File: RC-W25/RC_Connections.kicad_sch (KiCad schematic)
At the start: 26 parts, among them J1 USB_C_Receptacle_USB2.0_14P, SW3 Button, SW4 Button, U1 ESP32-C6-WROOM-1

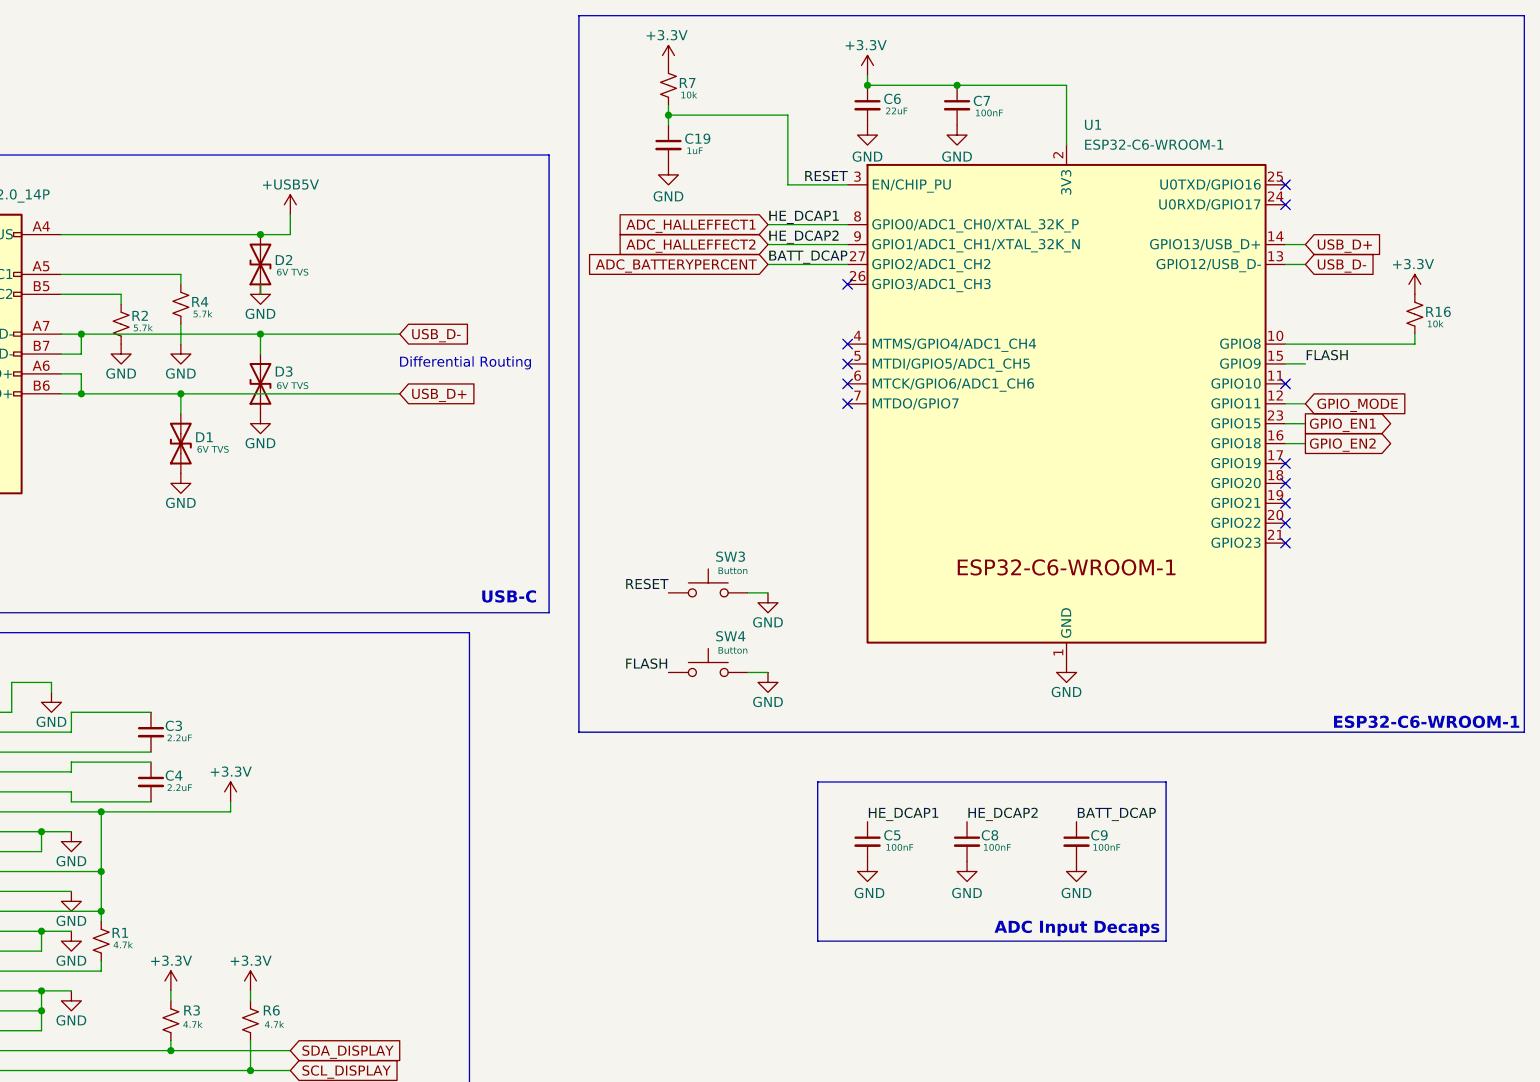
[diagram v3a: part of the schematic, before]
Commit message: Began Routing
Only need to spec out buttons before completion
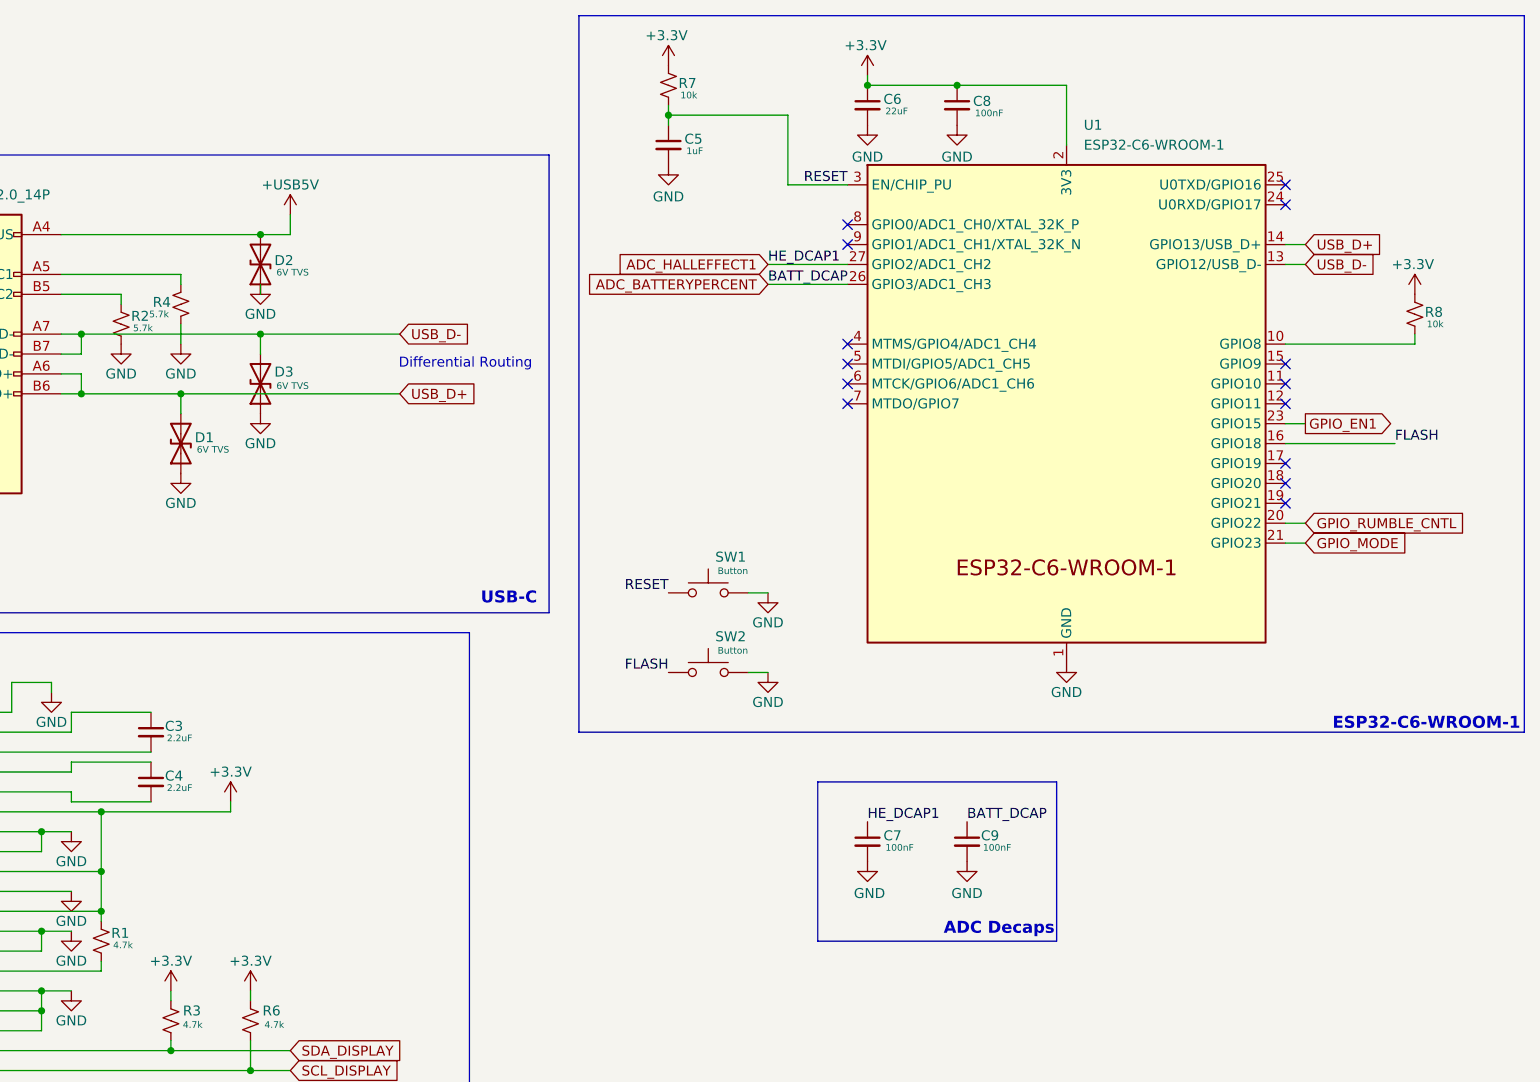
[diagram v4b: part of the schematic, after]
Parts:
- removed C8: 100nF, Capacitor_SMD:C_0402_1005Metric, symbol Device:C_Small
- R7: LCSC# C852861 -> C190095
- R8: renamed from R16; LCSC# C852861 -> C190095
- U1: footprint PCM_Espressif:ESP32-C6-WROOM-1 -> RF_Module:ESP32-C6-MINI-1
- renumbered C19 to C5, C5 to C7, C7 to C8, SW3 to SW1, SW4 to SW2
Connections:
- net GPIO_EN2 is gone; now on net FLASH: U1.16 (GPIO18)
- net ADC_BATTERYPERCENT: now also U1.26 (GPIO3/ADC1_CH3); no longer U1.27 (GPIO2/ADC1_CH2)
- net ADC_HALLEFFECT1: now also U1.27 (GPIO2/ADC1_CH2); no longer U1.8 (GPIO0/ADC1_CH0/XTAL_32K_P)
- net FLASH: no longer U1.15 (GPIO9)
- net GPIO_MODE: now also U1.21 (GPIO23); no longer U1.12 (GPIO11)
- net GPIO_RUMBLE_CNTL: now reaches U1.20 (GPIO22)
- net ADC_HALLEFFECT2: no longer names the net of U1.9 (GPIO1/ADC1_CH1/XTAL_32K_N)
- no-connect marks 14 -> 15
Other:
- note added: "ADC Decaps"
- note removed: "ADC Input Decaps"
- moved on the sheet: C9

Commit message: EM Custom RC V1
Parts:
- added H1, H2, H3, H4: MountingHole, MountingHole:MountingHole_2.2mm_M2, symbol Mechanical:MountingHole
- DS1: LCSC# (none) -> C2856808
- SW1, SW2: footprint (none) -> footprints:SW-SMD_L3.9-W3.0-P4.45; LCSC# (none) -> C720477
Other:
- note added: "MH"

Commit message: crc v1
finalized!! finally!! yes!!

- spec out 3.7V 1000mAh cell
- spec out ultra-thin coin motor

^make sure they have a jst-ph male connector or are organized to be ordered alongside one for manual soldering.
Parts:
- removed H1: MountingHole, MountingHole:MountingHole_2.2mm_M2, symbol Mechanical:MountingHole
- H1: renamed from H2; footprint MountingHole:MountingHole_2.2mm_M2 -> MountingHole:MountingHole_3.2mm_M3
- H2: renamed from H3; footprint MountingHole:MountingHole_2.2mm_M2 -> MountingHole:MountingHole_3.2mm_M3
- H3: renamed from H4; footprint MountingHole:MountingHole_2.2mm_M2 -> MountingHole:MountingHole_3.2mm_M3
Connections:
- net GPIO_EN1: now also U1.21 (GPIO23); no longer U1.23 (GPIO15)
- net GPIO_MODE: now also U1.20 (GPIO22); no longer U1.21 (GPIO23)
- net GPIO_RUMBLE_CNTL: now also U1.23 (GPIO15); no longer U1.20 (GPIO22)
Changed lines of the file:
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@@
 	(wire
 		(pts
-			(xy 234.95 69.85) (xy 220.98 69.85)
+			(xy 245.11 69.85) (xy 220.98 69.85)
 		)
 		(stroke
@@
 	)
 	(rectangle
-		(start 139.7 156.21)
+		(start 139.7 161.29)
 		(end 158.75 179.07)
 		(stroke
@@
 	)
 	(label "FLASH"
-		(at 234.95 69.85 0)
+		(at 245.11 69.85 0)
 		(effects
 			(font
@@
 		)
 	)
-	(global_label "GPIO_MODE"
+	(global_label "GPIO_RUMBLE_CNTL"
 		(shape input)
-		(at 223.52 82.55 0)
+		(at 223.52 67.31 0)
 		(fields_autoplaced yes)
 		(effects
@@
 		)
 		(property "Intersheetrefs" "${INTERSHEET_REFS}"
-			(at 237.149 82.55 0)
+			(at 245.0109 67.31 0)
 			(effects
 				(font
@@
 		)
 	)
-	(global_label "GPIO_EN1"
-		(shape output)
-		(at 223.52 67.31 0)
+	(global_label "SDA_DISPLAY"
+		(shape input)
+		(at 93.98 147.32 0)
 		(fields_autoplaced yes)
 		(effects
@@
 		)
 		(property "Intersheetrefs" "${INTERSHEET_REFS}"
-			(at 235.6371 67.31 0)
+			(at 109.0605 147.32 0)
 			(effects
 				(font
@@
 		)
 	)
-	(global_label "SDA_DISPLAY"
+	(global_label "GPIO_MODE"
 		(shape input)
-		(at 93.98 147.32 0)
+		(at 223.52 80.01 0)
 		(fields_autoplaced yes)
 		(effects
@@
 		)
 		(property "Intersheetrefs" "${INTERSHEET_REFS}"
-			(at 109.0605 147.32 0)
+			(at 237.149 80.01 0)
 			(effects
 				(font
@@
 		)
 	)
-	(global_label "GPIO_RUMBLE_CNTL"
-		(shape input)
-		(at 223.52 80.01 0)
+	(global_label "GPIO_EN1"
+		(shape output)
+		(at 223.52 82.55 0)
 		(fields_autoplaced yes)
 		(effects
@@
 		)
 		(property "Intersheetrefs" "${INTERSHEET_REFS}"
-			(at 245.0109 80.01 0)
+			(at 235.6371 82.55 0)
 			(effects
 				(font
@@
 		(dnp no)
 		(fields_autoplaced yes)
-		(property "Reference" "H4"
+		(property "Reference" "H3"
 			(at 144.78 172.7199 0)
 			(effects
@@
 			)
 		)
-		(property "Footprint" "MountingHole:MountingHole_2.2mm_M2"
+		(property "Footprint" "MountingHole:MountingHole_3.2mm_M3"
 			(at 142.24 173.99 0)
 			(effects
@@
 			(project "RC-W25"
 				(path "/427b2895-e3a6-4096-b101-5f65a3f7473e/01bd870e-4674-4257-9660-564635d632de"
-					(reference "H4")
+					(reference "H3")
 					(unit 1)
 				)
@@
 	)
 	(symbol
-		(lib_id "Mechanical:MountingHole")
-		(at 142.24 158.75 0)
-		(unit 1)
-		(exclude_from_sim yes)
-		(in_bom no)
-		(on_board yes)
-		(dnp no)
-		(fields_autoplaced yes)
-		(property "Reference" "H1"
-			(at 144.78 157.4799 0)
-			(effects
-				(font
-					(size 1.27 1.27)
-				)
-				(justify left)
-			)
-		)
-		(property "Value" "MountingHole"
-			(at 144.78 160.0199 0)
-			(effects
-				(font
-					(size 1.27 1.27)
-				)
-				(justify left)
-			)
-		)
-		(property "Footprint" "MountingHole:MountingHole_2.2mm_M2"
-			(at 142.24 158.75 0)
-			(effects
-				(font
-					(size 1.27 1.27)
-				)
-				(hide yes)
-			)
-		)
-		(property "Datasheet" "~"
-			(at 142.24 158.75 0)
-			(effects
-				(font
-					(size 1.27 1.27)
-				)
-				(hide yes)
-			)
-		)
-		(property "Description" "Mounting Hole without connection"
-			(at 142.24 158.75 0)
-			(effects
-				(font
-					(size 1.27 1.27)
-				)
-				(hide yes)
-			)
-		)
-		(instances
-			(project ""
-				(path "/427b2895-e3a6-4096-b101-5f65a3f7473e/01bd870e-4674-4257-9660-564635d632de"
-					(reference "H1")
-					(unit 1)
-				)
-			)
-		)
-	)
-	(symbol
 		(lib_id "Device:C_Small")
 		(at 142.24 31.75 0)
@@
 		(dnp no)
 		(fields_autoplaced yes)
-		(property "Reference" "H2"
+		(property "Reference" "H1"
 			(at 144.78 162.5599 0)
 			(effects
@@
 			)
 		)
-		(property "Footprint" "MountingHole:MountingHole_2.2mm_M2"
+		(property "Footprint" "MountingHole:MountingHole_3.2mm_M3"
 			(at 142.24 163.83 0)
 			(effects
@@
 			(project "RC-W25"
 				(path "/427b2895-e3a6-4096-b101-5f65a3f7473e/01bd870e-4674-4257-9660-564635d632de"
-					(reference "H2")
+					(reference "H1")
 					(unit 1)
 				)
@@
 		(dnp no)
 		(fields_autoplaced yes)
-		(property "Reference" "H3"
+		(property "Reference" "H2"
 			(at 144.78 167.6399 0)
 			(effects
@@
 			)
 		)
-		(property "Footprint" "MountingHole:MountingHole_2.2mm_M2"
+		(property "Footprint" "MountingHole:MountingHole_3.2mm_M3"
 			(at 142.24 168.91 0)
 			(effects
@@
 			(project "RC-W25"
 				(path "/427b2895-e3a6-4096-b101-5f65a3f7473e/01bd870e-4674-4257-9660-564635d632de"
-					(reference "H3")
+					(reference "H2")
 					(unit 1)
 				)

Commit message: crc v1
board complete and ready for assembly setup!
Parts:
- removed C5: 1uF, Capacitor_SMD:C_0805_2012Metric, symbol Device:C_Small
- removed U1: ESP32-C6-WROOM-1, RF_Module:ESP32-C6-MINI-1, symbol PCM_Espressif:ESP32-C6-WROOM-1
- added C9: 100nF, Capacitor_SMD:C_0402_1005Metric, symbol Device:C_Small
- added U1: ESP32-C6-MINI-1, RF_Module:ESP32-C6-MINI-1, symbol RF_Module:ESP32-C6-MINI-1
- C6: value 22uF -> 100nF; footprint Capacitor_SMD:C_0805_2012Metric -> Capacitor_SMD:C_0402_1005Metric; LCSC# C380337 -> C22435938
- C8: value 100nF -> 22uF; footprint Capacitor_SMD:C_0402_1005Metric -> Capacitor_SMD:C_0805_2012Metric; LCSC# C22435938 -> C380337
- renumbered C7 to C5, C9 to C7
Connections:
- net +3.3V: now also C9.1, U1.3 (3V3); no longer C6.1
- net ADC_BATTERYPERCENT: now also U1.6 (IO3)
- net ADC_HALLEFFECT1: now also U1.5 (IO2)
- net FLASH: now also U1.23 (IO9)
- net GND: now also C9.2, U1.1 (GND), U1.11 (GND), U1.12 (IO0), U1.13 (IO1), U1.14 (GND), U1.2 (GND), U1.36 (GND), U1.37 (GND), U1.38 (GND), U1.39 (GND), U1.40 (GND), U1.41 (GND), U1.42 (GND), U1.43 (GND), U1.44 (GND), U1.45 (GND), U1.46 (GND), U1.47 (GND), U1.48 (GND), U1.49 (GND), U1.50 (GND), U1.51 (GND), U1.52 (GND), U1.53 (GND)
- net GPIO_EN1: now also U1.28 (IO22)
- net GPIO_MODE: now also U1.9 (IO4)
- net RESET: now also C6.1, U1.8 (EN)
- net USB_D+: now also U1.18 (IO13)
- net USB_D-: now also U1.17 (IO12)
- net at R8.2: now also U1.22 (IO8)
- no-connect marks 15 -> 13
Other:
- note added: "ESP32-C6-MINI-1"
- note removed: "ESP32-C6-WROOM-1"
- moved on the sheet: C5, C7, H1, H2, H3, SW1, SW2

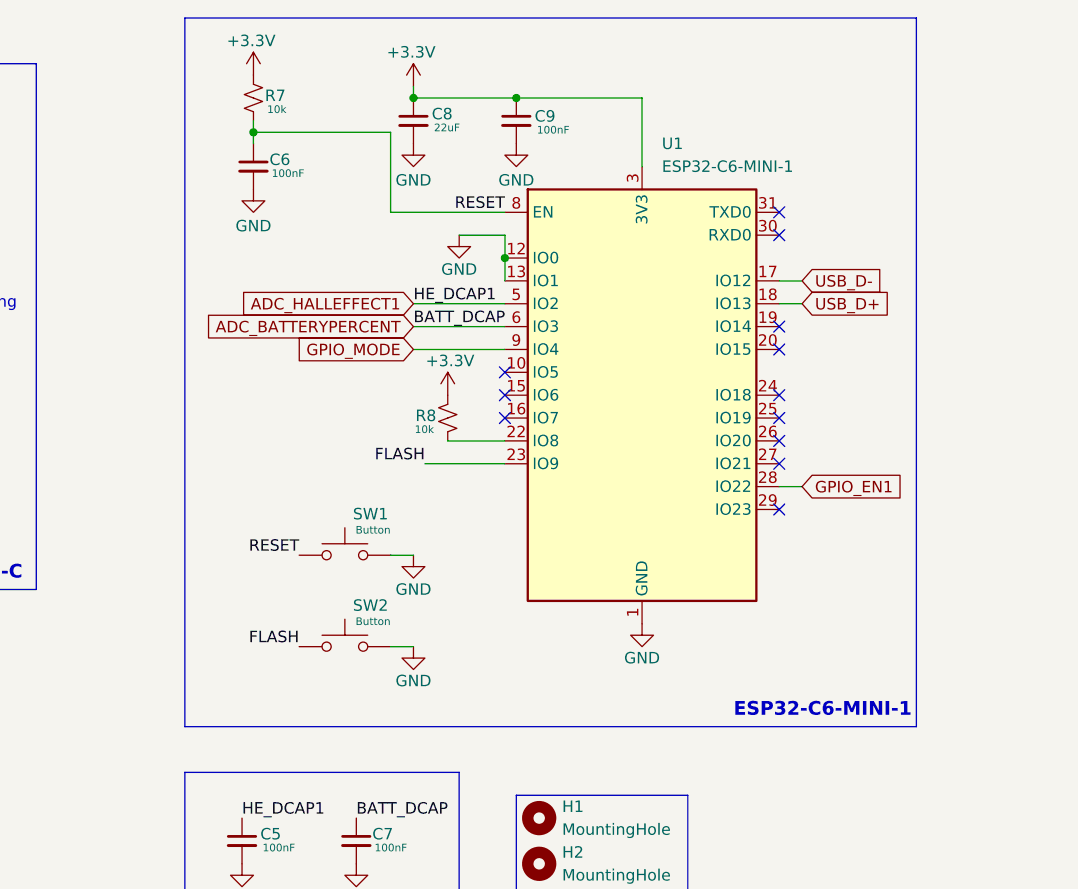
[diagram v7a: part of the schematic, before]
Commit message: crc v1
board complete and ready for assembly setup
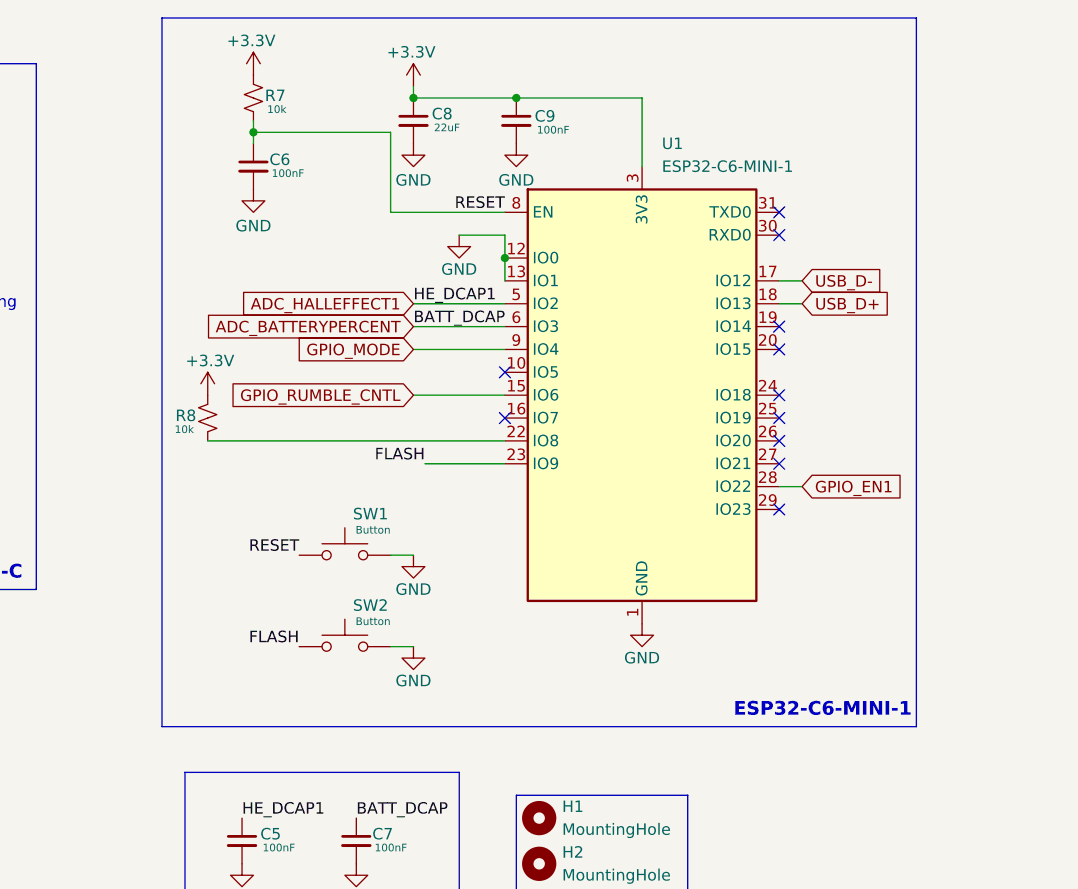
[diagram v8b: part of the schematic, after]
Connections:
- net GPIO_RUMBLE_CNTL: now reaches U1.15 (IO6)
- no-connect marks 13 -> 12
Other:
- moved on the sheet: R8
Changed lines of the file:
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@@
 	)
 	(no_connect
-		(at 179.07 69.85)
-	)
-	(no_connect
 		(at 179.07 72.39)
 	)
@@
 	(wire
 		(pts
-			(xy 172.72 74.93) (xy 179.07 74.93)
+			(xy 146.05 74.93) (xy 179.07 74.93)
 		)
 		(stroke
@@
 	(wire
 		(pts
+			(xy 168.91 69.85) (xy 179.07 69.85)
+		)
+		(stroke
+			(width 0)
+			(type default)
+		)
+	)
+	(wire
+		(pts
 			(xy 66.04 111.76) (xy 66.04 110.49)
 		)
@@
 	)
 	(rectangle
-		(start 143.51 27.94)
+		(start 140.97 27.94)
 		(end 224.79 106.68)
 		(stroke
@@
 		)
 	)
+	(global_label "GPIO_RUMBLE_CNTL"
+		(shape input)
+		(at 168.91 69.85 180)
+		(fields_autoplaced yes)
+		(effects
+			(font
+				(size 1.27 1.27)
+			)
+			(justify right)
+		)
+		(property "Intersheetrefs" "${INTERSHEET_REFS}"
+			(at 147.4191 69.85 0)
+			(effects
+				(font
+					(size 1.27 1.27)
+				)
+				(justify right)
+				(hide yes)
+			)
+		)
+	)
 	(global_label "SCL_DISPLAY"
 		(shape input)
@@
 	(symbol
 		(lib_id "Device:R_Small_US")
-		(at 172.72 72.39 0)
+		(at 146.05 72.39 0)
 		(mirror y)
 		(unit 1)
@@
 		(dnp no)
 		(property "Reference" "R8"
-			(at 171.45 72.136 0)
+			(at 144.78 72.136 0)
 			(effects
 				(font
@@
 		)
 		(property "Value" "10k"
-			(at 171.196 73.66 0)
+			(at 144.526 73.66 0)
 			(effects
 				(font
@@
 		)
 		(property "Footprint" "Resistor_SMD:R_0402_1005Metric"
-			(at 172.72 72.39 0)
+			(at 146.05 72.39 0)
 			(effects
 				(font
@@
 		)
 		(property "Datasheet" "https://www.lcsc.com/datasheet/lcsc_datasheet_2304140030_YAGEO-RT0402BRD0710KL_C190095.pdf"
-			(at 172.72 72.39 0)
+			(at 146.05 72.39 0)
 			(effects
 				(font
@@
 		)
 		(property "Description" "Resistor, small US symbol"
-			(at 172.72 72.39 0)
+			(at 146.05 72.39 0)
 			(effects
 				(font
@@
 		)
 		(property "LCSC#" "C190095"
-			(at 172.72 72.39 0)
+			(at 146.05 72.39 0)
 			(effects
 				(font
@@
 	(symbol
 		(lib_id "power:+3.3V")
-		(at 172.72 69.85 0)
+		(at 146.05 69.85 0)
 		(mirror y)
 		(unit 1)
@@
 		(dnp no)
 		(property "Reference" "#PWR026"
-			(at 172.72 73.66 0)
+			(at 146.05 73.66 0)
 			(effects
 				(font
@@
 		)
 		(property "Value" "+3.3V"
-			(at 172.974 66.04 0)
+			(at 146.304 66.04 0)
 			(effects
 				(font
@@
 		)
 		(property "Footprint" ""
-			(at 172.72 69.85 0)
+			(at 146.05 69.85 0)
 			(effects
 				(font
@@
 		)
 		(property "Datasheet" ""
-			(at 172.72 69.85 0)
+			(at 146.05 69.85 0)
 			(effects
 				(font
@@
 		)
 		(property "Description" "Power symbol creates a global label with name \"+3.3V\""
-			(at 172.72 69.85 0)
+			(at 146.05 69.85 0)
 			(effects
 				(font
